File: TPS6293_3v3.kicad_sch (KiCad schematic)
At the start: 15 parts

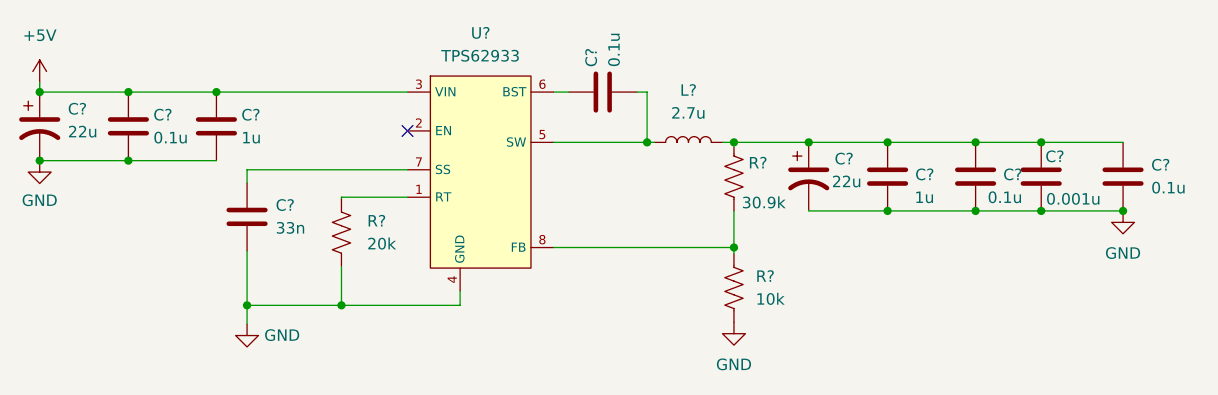
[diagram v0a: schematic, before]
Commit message: fixing sheet numbers and adding schematic PDF
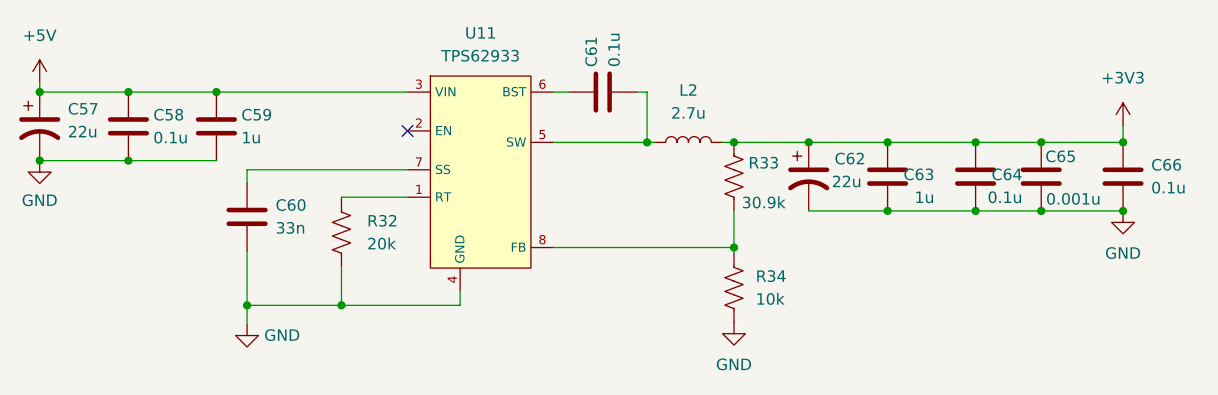
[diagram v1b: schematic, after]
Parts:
- gave numbers to parts that had none: 15
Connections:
- net +3V3: now reaches C62.1, C63.1, C64.1, C65.1, C66.1, L2.2, R33.1
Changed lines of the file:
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@@
   (junction (at 191.9478 97.3074) (diameter 0) (color 0 0 0 0)
+  )
+  (junction (at 208.3308 97.3074) (diameter 0) (color 0 0 0 0)
   )
   (junction (at 182.1688 97.3074) (diameter 0) (color 0 0 0 0)
@@
     (stroke (width 0) (type default) (color 0 0 0 0))
   )
+  (wire (pts (xy 208.3308 95.4786) (xy 208.3308 97.3074))
+    (stroke (width 0) (type default) (color 0 0 0 0))
+  )
   (wire (pts (xy 145.0848 108.9914) (xy 165.1 108.9914))
     (stroke (width 0) (type default) (color 0 0 0 0))
@@
   (symbol (lib_id "Device:C") (at 110.998 105.5878 0) (unit 1)
     (in_bom yes) (on_board yes) (fields_autoplaced)
-    (property "Reference" "C?" (id 0) (at 114.173 104.3177 0)
+    (property "Reference" "C60" (id 0) (at 114.173 104.3177 0)
       (effects (font (size 1.27 1.27)) (justify left))
     )
@@
   (symbol (lib_id "power:GND") (at 208.3308 104.9274 0) (unit 1)
     (in_bom yes) (on_board yes) (fields_autoplaced)
-    (property "Reference" "#PWR?" (id 0) (at 208.3308 111.2774 0)
+    (property "Reference" "#PWR081" (id 0) (at 208.3308 111.2774 0)
       (effects (font (size 1.27 1.27)) hide)
     )
@@
     (pin "1")
   )
+  (symbol (lib_id "power:+3V3") (at 208.3308 95.4786 0) (unit 1)
+    (in_bom yes) (on_board yes) (fields_autoplaced)
+    (property "Reference" "#PWR080" (id 0) (at 208.3308 99.2886 0)
+      (effects (font (size 1.27 1.27)) hide)
+    )
+    (property "Value" "+3V3" (id 1) (at 208.3308 90.17 0))
+    (property "Footprint" "" (id 2) (at 208.3308 95.4786 0)
+      (effects (font (size 1.27 1.27)) hide)
+    )
+    (property "Datasheet" "" (id 3) (at 208.3308 95.4786 0)
+      (effects (font (size 1.27 1.27)) hide)
+    )
+    (pin "1")
+  )
   (symbol (lib_id "Device:C") (at 182.1688 101.1174 0) (mirror y) (unit 1)
     (in_bom yes) (on_board yes)
-    (property "Reference" "C?" (id 0) (at 187.3758 100.9142 0)
+    (property "Reference" "C63" (id 0) (at 187.3758 100.9142 0)
       (effects (font (size 1.27 1.27)) (justify left))
     )
@@
   (symbol (lib_id "Device:C") (at 208.3308 101.1174 0) (unit 1)
     (in_bom yes) (on_board yes) (fields_autoplaced)
-    (property "Reference" "C?" (id 0) (at 211.455 99.8473 0)
+    (property "Reference" "C66" (id 0) (at 211.455 99.8473 0)
       (effects (font (size 1.27 1.27)) (justify left))
     )
@@
   (symbol (lib_id "Power:TPS62933") (at 137.4648 100.1014 0) (unit 1)
     (in_bom yes) (on_board yes) (fields_autoplaced)
-    (property "Reference" "U?" (id 0) (at 136.9568 85.1916 0))
+    (property "Reference" "U11" (id 0) (at 136.9568 85.1916 0))
     (property "Value" "TPS62933" (id 1) (at 136.9568 87.7316 0))
     (property "Footprint" "" (id 2) (at 137.7188 116.6114 0)
@@
   (symbol (lib_id "Device:C") (at 199.2376 101.1174 0) (unit 1)
     (in_bom yes) (on_board yes)
-    (property "Reference" "C?" (id 0) (at 199.6948 98.9076 0)
+    (property "Reference" "C65" (id 0) (at 199.6948 98.9076 0)
       (effects (font (size 1.27 1.27)) (justify left))
     )
@@
   (symbol (lib_id "Device:C_Polarized_US") (at 173.4058 101.1174 0) (unit 1)
     (in_bom yes) (on_board yes)
-    (property "Reference" "C?" (id 0) (at 176.276 99.1616 0)
+    (property "Reference" "C62" (id 0) (at 176.276 99.1616 0)
       (effects (font (size 1.27 1.27)) (justify left))
     )
@@
   (symbol (lib_id "Device:C") (at 191.9478 101.1174 0) (mirror y) (unit 1)
     (in_bom yes) (on_board yes)
-    (property "Reference" "C?" (id 0) (at 197.1548 100.9142 0)
+    (property "Reference" "C64" (id 0) (at 197.1548 100.9142 0)
       (effects (font (size 1.27 1.27)) (justify left))
     )
@@
   (symbol (lib_id "Device:R_US") (at 165.1 101.1174 0) (unit 1)
     (in_bom yes) (on_board yes)
-    (property "Reference" "R?" (id 0) (at 166.7002 99.6188 0)
+    (property "Reference" "R33" (id 0) (at 166.7002 99.6188 0)
       (effects (font (size 1.27 1.27)) (justify left))
     )
@@
   (symbol (lib_id "Device:C_Polarized_US") (at 87.9602 95.5294 0) (unit 1)
     (in_bom yes) (on_board yes) (fields_autoplaced)
-    (property "Reference" "C?" (id 0) (at 91.0844 93.6243 0)
+    (property "Reference" "C57" (id 0) (at 91.0844 93.6243 0)
       (effects (font (size 1.27 1.27)) (justify left))
     )
@@
   (symbol (lib_id "Device:R_US") (at 121.4882 107.3404 0) (unit 1)
     (in_bom yes) (on_board yes) (fields_autoplaced)
-    (property "Reference" "R?" (id 0) (at 124.333 106.0703 0)
+    (property "Reference" "R32" (id 0) (at 124.333 106.0703 0)
       (effects (font (size 1.27 1.27)) (justify left))
     )
@@
   (symbol (lib_id "power:+5V") (at 87.9602 90.7034 0) (unit 1)
     (in_bom yes) (on_board yes) (fields_autoplaced)
-    (property "Reference" "#PWR?" (id 0) (at 87.9602 94.5134 0)
+    (property "Reference" "#PWR076" (id 0) (at 87.9602 94.5134 0)
       (effects (font (size 1.27 1.27)) hide)
     )
@@
   (symbol (lib_id "power:GND") (at 110.998 117.5004 0) (unit 1)
     (in_bom yes) (on_board yes) (fields_autoplaced)
-    (property "Reference" "#PWR?" (id 0) (at 110.998 123.8504 0)
+    (property "Reference" "#PWR078" (id 0) (at 110.998 123.8504 0)
       (effects (font (size 1.27 1.27)) hide)
     )
@@
   (symbol (lib_id "Device:C") (at 150.5204 91.7194 90) (unit 1)
     (in_bom yes) (on_board yes)
-    (property "Reference" "C?" (id 0) (at 149.2758 88.9508 0)
+    (property "Reference" "C61" (id 0) (at 149.2758 88.9508 0)
       (effects (font (size 1.27 1.27)) (justify left))
     )
@@
   (symbol (lib_id "power:GND") (at 165.1 117.2972 0) (unit 1)
     (in_bom yes) (on_board yes) (fields_autoplaced)
-    (property "Reference" "#PWR?" (id 0) (at 165.1 123.6472 0)
+    (property "Reference" "#PWR079" (id 0) (at 165.1 123.6472 0)
       (effects (font (size 1.27 1.27)) hide)
     )
@@
   (symbol (lib_id "Device:R_US") (at 165.1 113.4872 0) (unit 1)
     (in_bom yes) (on_board yes) (fields_autoplaced)
-    (property "Reference" "R?" (id 0) (at 167.513 112.2171 0)
+    (property "Reference" "R34" (id 0) (at 167.513 112.2171 0)
       (effects (font (size 1.27 1.27)) (justify left))
     )
@@
   (symbol (lib_id "power:GND") (at 87.9602 99.3394 0) (unit 1)
     (in_bom yes) (on_board yes) (fields_autoplaced)
-    (property "Reference" "#PWR?" (id 0) (at 87.9602 105.6894 0)
+    (property "Reference" "#PWR077" (id 0) (at 87.9602 105.6894 0)
       (effects (font (size 1.27 1.27)) hide)
     )
@@
   (symbol (lib_id "Device:C") (at 97.8154 95.5294 0) (unit 1)
     (in_bom yes) (on_board yes)
-    (property "Reference" "C?" (id 0) (at 100.584 94.2848 0)
+    (property "Reference" "C58" (id 0) (at 100.584 94.2848 0)
       (effects (font (size 1.27 1.27)) (justify left))
     )
@@
   (symbol (lib_id "Device:C") (at 107.5944 95.5294 0) (unit 1)
     (in_bom yes) (on_board yes)
-    (property "Reference" "C?" (id 0) (at 110.363 94.2848 0)
+    (property "Reference" "C59" (id 0) (at 110.363 94.2848 0)
       (effects (font (size 1.27 1.27)) (justify left))
     )
@@
   (symbol (lib_id "Device:L") (at 160.0454 97.3074 90) (unit 1)
     (in_bom yes) (on_board yes) (fields_autoplaced)
-    (property "Reference" "L?" (id 0) (at 160.0454 91.5416 90))
+    (property "Reference" "L2" (id 0) (at 160.0454 91.5416 90))
     (property "Value" "2.7u" (id 1) (at 160.0454 94.0816 90))
     (property "Footprint" "" (id 2) (at 160.0454 97.3074 0)

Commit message: Fixing ERC
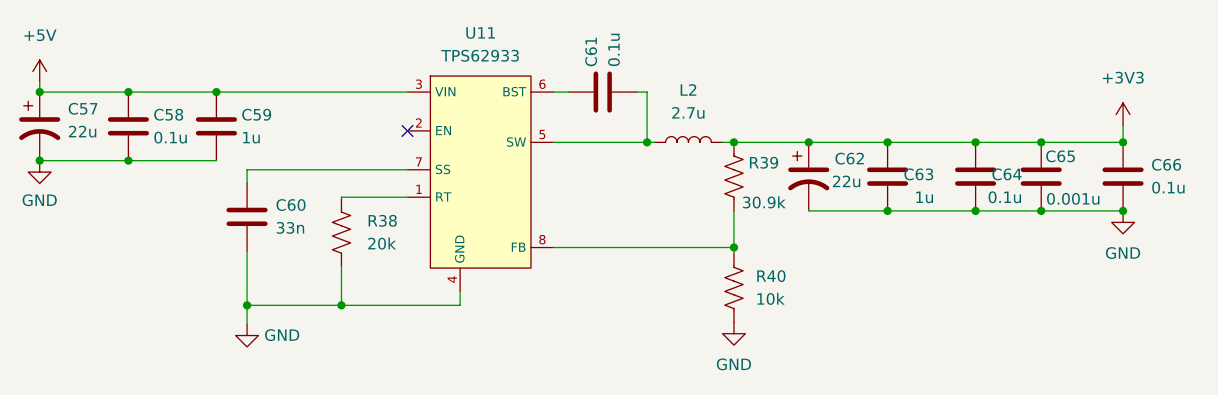
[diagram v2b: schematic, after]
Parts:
- renumbered R32 to R38, R33 to R39, R34 to R40
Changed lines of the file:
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@@
   (symbol (lib_id "power:GND") (at 208.3308 104.9274 0) (unit 1)
     (in_bom yes) (on_board yes) (fields_autoplaced)
-    (property "Reference" "#PWR081" (id 0) (at 208.3308 111.2774 0)
+    (property "Reference" "#PWR084" (id 0) (at 208.3308 111.2774 0)
       (effects (font (size 1.27 1.27)) hide)
     )
@@
   (symbol (lib_id "power:+3V3") (at 208.3308 95.4786 0) (unit 1)
     (in_bom yes) (on_board yes) (fields_autoplaced)
-    (property "Reference" "#PWR080" (id 0) (at 208.3308 99.2886 0)
+    (property "Reference" "#PWR083" (id 0) (at 208.3308 99.2886 0)
       (effects (font (size 1.27 1.27)) hide)
     )
@@
   (symbol (lib_id "Device:R_US") (at 165.1 101.1174 0) (unit 1)
     (in_bom yes) (on_board yes)
-    (property "Reference" "R33" (id 0) (at 166.7002 99.6188 0)
+    (property "Reference" "R39" (id 0) (at 166.7002 99.6188 0)
       (effects (font (size 1.27 1.27)) (justify left))
     )
@@
   (symbol (lib_id "Device:R_US") (at 121.4882 107.3404 0) (unit 1)
     (in_bom yes) (on_board yes) (fields_autoplaced)
-    (property "Reference" "R32" (id 0) (at 124.333 106.0703 0)
+    (property "Reference" "R38" (id 0) (at 124.333 106.0703 0)
       (effects (font (size 1.27 1.27)) (justify left))
     )
@@
   (symbol (lib_id "power:+5V") (at 87.9602 90.7034 0) (unit 1)
     (in_bom yes) (on_board yes) (fields_autoplaced)
-    (property "Reference" "#PWR076" (id 0) (at 87.9602 94.5134 0)
+    (property "Reference" "#PWR079" (id 0) (at 87.9602 94.5134 0)
       (effects (font (size 1.27 1.27)) hide)
     )
@@
   (symbol (lib_id "power:GND") (at 110.998 117.5004 0) (unit 1)
     (in_bom yes) (on_board yes) (fields_autoplaced)
-    (property "Reference" "#PWR078" (id 0) (at 110.998 123.8504 0)
+    (property "Reference" "#PWR081" (id 0) (at 110.998 123.8504 0)
       (effects (font (size 1.27 1.27)) hide)
     )
@@
   (symbol (lib_id "power:GND") (at 165.1 117.2972 0) (unit 1)
     (in_bom yes) (on_board yes) (fields_autoplaced)
-    (property "Reference" "#PWR079" (id 0) (at 165.1 123.6472 0)
+    (property "Reference" "#PWR082" (id 0) (at 165.1 123.6472 0)
       (effects (font (size 1.27 1.27)) hide)
     )
@@
   (symbol (lib_id "Device:R_US") (at 165.1 113.4872 0) (unit 1)
     (in_bom yes) (on_board yes) (fields_autoplaced)
-    (property "Reference" "R34" (id 0) (at 167.513 112.2171 0)
+    (property "Reference" "R40" (id 0) (at 167.513 112.2171 0)
       (effects (font (size 1.27 1.27)) (justify left))
     )
@@
   (symbol (lib_id "power:GND") (at 87.9602 99.3394 0) (unit 1)
     (in_bom yes) (on_board yes) (fields_autoplaced)
-    (property "Reference" "#PWR077" (id 0) (at 87.9602 105.6894 0)
-      (effects (font (size 1.27 1.27)) hide)
-    )
+    (property "Reference" "#PWR080" (id 0) (at 87.9602 105.6894 0)
+      (effects (font (size 1.27 1.27)) hide)
+    )
